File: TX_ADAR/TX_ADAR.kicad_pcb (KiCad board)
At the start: 4 copper layers, 68 x 156.9 mm, 58 parts, among them IC1 REG1117A-1.8, IC2 REG1117A-2.5, J1 Screw_Terminal_01x02, J10 Conn_Coaxial, J11 RJ45_LED_Shielded, J12 RJ45_LED_Shielded, J16 RJ45_LED_Shielded, J2 Conn_Coaxial, J21 Conn_01x04, J3 Conn_Coaxial, J4 Conn_Coaxial, J5 Conn_Coaxial, J6 Conn_Coaxial, J7 Conn_Coaxial, J8 Conn_Coaxial, J9 Conn_Coaxial, SW1 SW_SPDT, SW2 SW_SPDT, SW3 SW_SPDT, SW9 SW_SPDT, U10 TXB0101DBV, U11 TXB0101DBV, U14 TXB0101DBV, U19 TXB0101DBV, U2 ADAR2001ACCZ

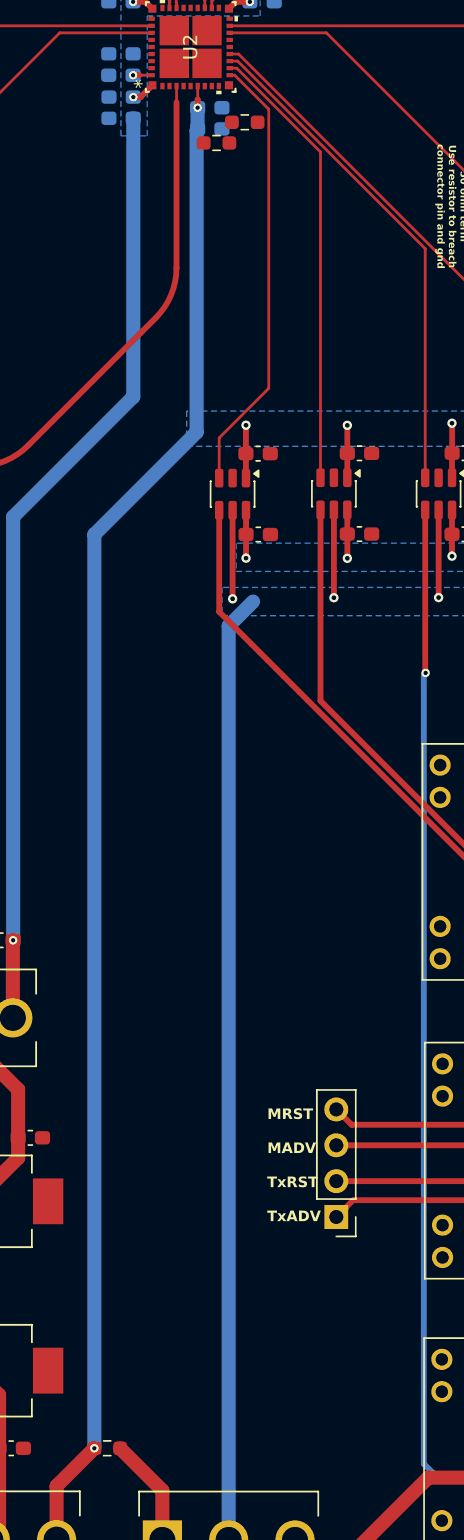
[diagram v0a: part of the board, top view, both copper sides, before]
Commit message: Added Level Shifters
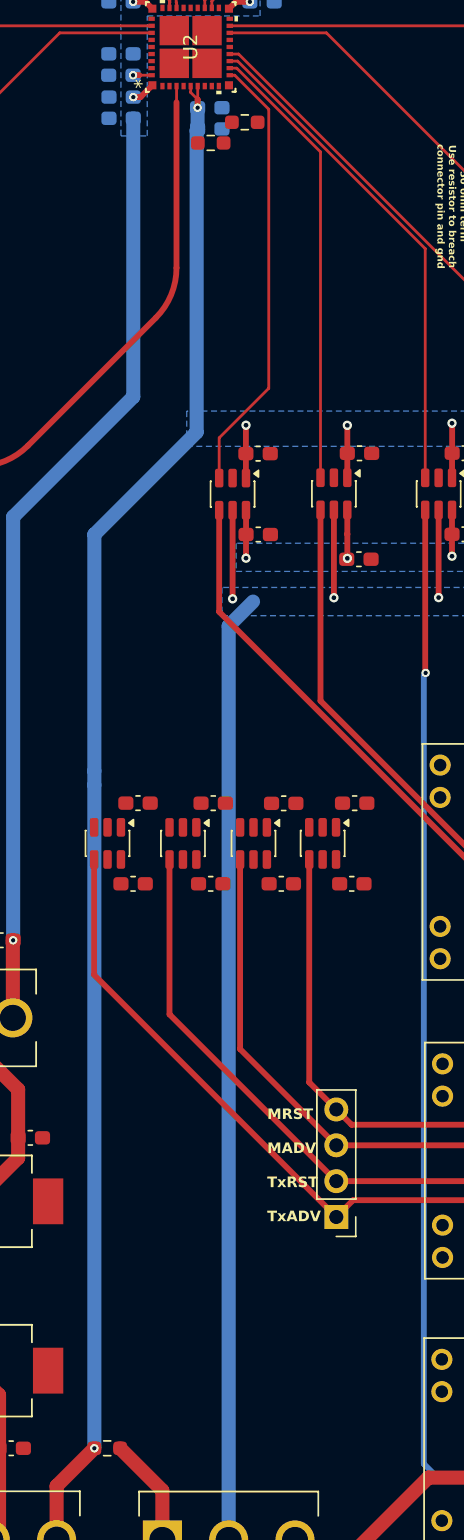
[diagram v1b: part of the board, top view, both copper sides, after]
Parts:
- removed C25: 100nF, Capacitor_SMD:C_0603_1608Metric_Pad1.08x0.95mm_HandSolder
- added C19: 100nF, Capacitor_SMD:C_0603_1608Metric_Pad1.08x0.95mm_HandSolder, F.Cu at (133.7, 113.8)
- added C20: 100nF, Capacitor_SMD:C_0603_1608Metric_Pad1.08x0.95mm_HandSolder, F.Cu at (133.5, 119.5)
- added C21: 100nF, Capacitor_SMD:C_0603_1608Metric_Pad1.08x0.95mm_HandSolder, F.Cu at (128.7, 113.8)
- added C22: 100nF, Capacitor_SMD:C_0603_1608Metric_Pad1.08x0.95mm_HandSolder, F.Cu at (128.5, 119.5)
- added C27: 100nF, Capacitor_SMD:C_0603_1608Metric_Pad1.08x0.95mm_HandSolder, F.Cu at (123.7, 113.8)
- added C28: 100nF, Capacitor_SMD:C_0603_1608Metric_Pad1.08x0.95mm_HandSolder, F.Cu at (123.5, 119.5)
- added C30: 100nF, Capacitor_SMD:C_0603_1608Metric_Pad1.08x0.95mm_HandSolder, F.Cu at (134.0, 96.5)
- added C38: 100nF, Capacitor_SMD:C_0603_1608Metric_Pad1.08x0.95mm_HandSolder, F.Cu at (118.0, 119.5)
- added C41: 100nF, Capacitor_SMD:C_0603_1608Metric_Pad1.08x0.95mm_HandSolder, F.Cu at (118.3, 113.8)
- added U15: TXB0101DBV, Package_TO_SOT_SMD:SOT-23-6, F.Cu at (116.2, 116.6)
- added U16: TXB0101DBV, Package_TO_SOT_SMD:SOT-23-6, F.Cu at (121.5, 116.6)
- added U17: TXB0101DBV, Package_TO_SOT_SMD:SOT-23-6, F.Cu at (126.5, 116.6)
- added U18: TXB0101DBV, Package_TO_SOT_SMD:SOT-23-6, F.Cu at (131.4, 116.6)
- moved R5 0.41 mm to (123.5, 67.0)
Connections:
- J10 pad 4: GND -> (no net)
- J3 pad 4: GND -> (no net)
- J4 pad 4: GND -> (no net)
- J5 pad 4: GND -> (no net)
- J6 pad 4: GND -> (no net)
- J7 pad 4: GND -> (no net)
- J8 pad 4: GND -> (no net)
- J9 pad 4: GND -> (no net)
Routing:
- net /External Input/TxADV: track 13.2 -> 45.6 mm
- net /External Input/TxRST: track 12.4 -> 40.1 mm
- net /External Input/MADV: track 12.6 -> 35.7 mm
- net /External Input/MRST: track 12.8 -> 31.3 mm
- net +1V8: track 130.6 -> 131.8 mm

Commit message: Changed State Machine Level Shifters Location
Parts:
- moved J16 24.9 mm to (171.4, 133.9)
- moved U15 22.6 mm to (123.9, 137.9), turned to 0 degrees
- moved C41 22.1 mm to (121.0, 135.7), turned to 90 degrees
- moved C38 18.7 mm to (126.7, 136.1), turned to 90 degrees
- moved C27 16.8 mm to (121.0, 130.4), turned to 90 degrees
- moved U16 16.1 mm to (123.9, 132.6), turned to 0 degrees
- moved J21 15.6 mm to (148.0, 143.1)
- moved C19 14.3 mm to (121.0, 120.4), turned to 90 degrees
- moved C21 13.9 mm to (121.0, 125.4), turned to 90 degrees
- moved C28 11.5 mm to (126.7, 130.6), turned to 90 degrees
- moved U17 11.2 mm to (123.9, 127.5), turned to 0 degrees
- moved U18 9.67 mm to (123.9, 122.7), turned to 0 degrees
- moved C20 6.86 mm to (126.7, 120.6), turned to 90 degrees
- moved C22 6.34 mm to (126.7, 125.6), turned to 90 degrees
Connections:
- J16 pad 1: GND -> (no net)
- J16 pad 10: unconnected-(J16-Pad10) -> (no net)
- J16 pad 11: unconnected-(J16-Pad11) -> (no net)
- J16 pad 12: unconnected-(J16-Pad12) -> (no net)
- J16 pad 2: /External Input/MRST -> (no net)
- J16 pad 3: GND -> (no net)
- J16 pad 4: /External Input/MADV -> (no net)
- J16 pad 5: GND -> (no net)
- J16 pad 6: /External Input/TxRST -> (no net)
- J16 pad 7: GND -> (no net)
- J16 pad 8: /External Input/TxADV -> (no net)
- J16 pad 9: unconnected-(J16-Pad9) -> (no net)
- J16 pad SH: GND -> (no net)
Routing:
- net /External Input/TxADV: track 45.6 -> 0.00 mm
- net /External Input/TxRST: track 40.1 -> 0.00 mm
- net /External Input/MADV: track 35.7 -> 0.00 mm
- net /External Input/MRST: track 31.3 -> 0.00 mm
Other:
- board text added: "Potentially won't use"

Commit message: Finding Location for State Machine Level Shifters
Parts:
- C19, C20, C21, C22, C27, C28, C38, C41, U15, U16, U17, U18: moved to B.Cu
- moved C38 45.8 mm to (97.3, 101.0)
- moved U15 42.1 mm to (100.2, 103.1), turned to 180 degrees
- moved C41 39.1 mm to (103.1, 101.0)
- moved C28 38.3 mm to (97.3, 106.0)
- moved U16 34.1 mm to (100.2, 108.0), turned to 180 degrees
- moved C22 32.8 mm to (97.3, 111.0)
- moved C27 30.3 mm to (103.1, 106.0)
- moved C20 29.7 mm to (97.3, 116.3)
- moved U17 27.8 mm to (100.2, 113.0), turned to 180 degrees
- moved U18 24.0 mm to (100.2, 118.3), turned to 180 degrees
- moved C21 23.1 mm to (103.1, 110.9)
- moved C19 18.3 mm to (103.1, 116.3)
- moved TP3 2.52 mm to (96.0, 166.0)
- moved TP4 2.52 mm to (96.0, 139.5)
- moved J21 0.50 mm to (148.5, 143.0)
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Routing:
- net /External Input/3V3_VCCB_SPI: track 86.2 -> 237.6 mm
- net /External Input/TxADV: track 0.00 -> 83.1 mm, vias 0 -> 1
- net /External Input/TxRST: track 0.00 -> 76.0 mm, vias 0 -> 1
- net /External Input/MADV: track 0.00 -> 68.9 mm, vias 0 -> 1
- net /External Input/MRST: track 0.00 -> 59.2 mm, vias 0 -> 1
- net +1V8: track 131.8 -> 174.4 mm
- net /SPI Communications/OE: track 92.2 -> 128.2 mm, vias 4 -> 9
- net /TxADV: track 0.00 -> 3.70 mm, vias 0 -> 1
- net /TxRST: track 0.00 -> 3.67 mm, vias 0 -> 1
- net /MADV: track 0.00 -> 3.67 mm, vias 0 -> 1
- net /MRST: track 0.00 -> 3.60 mm, vias 0 -> 1
- net Net-(SW2-A): track 9.71 -> 7.19 mm
- net Net-(SW9-A): track 13.2 -> 12.2 mm
- added copper zone on F.Cu, net /SPI Communications/OE
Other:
- board text added: "MADV"
- board text added: "MRST"
- board text added: "TxADV"
- board text added: "TxRST"

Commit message: Updated Spacing and Layout
Added Ethernet connection back to state machines.
Did some knockouts for the text on the Silkscreen
Left a comment about asking if via could be placed on component pad. (Don't think it should be)
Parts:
- moved J16 25.0 mm to (146.5, 136.4)
- moved J21 16.5 mm to (132.0, 143.0)
- moved C32 2.50 mm to (108.6, 126.5)
- moved SW9 2.50 mm to (104.8, 131.5)
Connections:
- J16 pad 1: (no net) -> GND
- J16 pad 10: (no net) -> unconnected-(J16-Pad10)
- J16 pad 11: (no net) -> unconnected-(J16-Pad11)
- J16 pad 12: (no net) -> unconnected-(J16-Pad12)
- J16 pad 2: (no net) -> /External Input/MRST
- J16 pad 3: (no net) -> GND
- J16 pad 4: (no net) -> /External Input/MADV
- J16 pad 5: (no net) -> GND
- J16 pad 6: (no net) -> /External Input/TxRST
- J16 pad 7: (no net) -> GND
- J16 pad 8: (no net) -> /External Input/TxADV
- J16 pad 9: (no net) -> unconnected-(J16-Pad9)
- J16 pad SH: (no net) -> GND
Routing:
- net /External Input/TxADV: track 83.1 -> 80.2 mm
- net /External Input/TxRST: track 76.0 -> 73.3 mm
- net Net-(SW9-A): track 12.2 -> 9.69 mm
- net Net-(IC2-VOUT): track 17.0 -> 14.5 mm
- net +2V5: track 73.7 -> 76.2 mm
- net /External Input/MADV: track 68.9 -> 66.4 mm
- net /External Input/MRST: track 59.2 -> 56.9 mm
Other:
- board text added: "*Ask about *Vias shouldn't be on component pad right?"
- board text added: "3V3 Power & CSB"
- board text added: "5V In"
- board text added: "GND"
- board text added: "SPI Communication"
- board text added: "State Machines"
- board text removed: "MADV"
- board text removed: "MRST"
- board text removed: "TxADV"
- board text removed: "TxRST"

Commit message: Fixed tracks & added images to schem
NEED: Find 50 ohm impedance width for OSH Park
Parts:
- moved J12 1.64 mm to (146.6, 116.0)
- moved C8 0.25 mm to (123.2, 64.5)
- moved C9 0.25 mm to (123.2, 66.0)
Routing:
- net /MRST: track 3.60 -> 46.2 mm
- net /MADV: track 3.67 -> 40.4 mm
- net /TxRST: track 3.67 -> 35.0 mm
- net /TxADV: track 3.70 -> 29.7 mm
- net +2V5: track 76.2 -> 95.7 mm
- net /External Input/3V3_SCLK: track 35.6 -> 38.4 mm
- net +1V8: track 174.4 -> 172.0 mm
- net /External Input/3V3_SDIO: track 31.3 -> 33.1 mm
- net /External Input/3V3SDO: track 30.5 -> 32.2 mm
- removed copper zone on B.Cu, net +2V5
